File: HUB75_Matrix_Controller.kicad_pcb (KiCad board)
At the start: 4 copper layers, 59 x 53 mm, 52 parts, among them J1 USB_C_Receptacle_USB2.0_16P, J2 Barrel_Jack_MountingPin, J3 Screw_Terminal_01x02, J4 Micro_SD_Card_Det2, J5 SFH11-PBPC-D08-ST-BK, SW1 EN, SW2 BOOT, U1 LSM6DSOTR, U2 AMS1117-3.3, U3 USBLC6-2SC6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

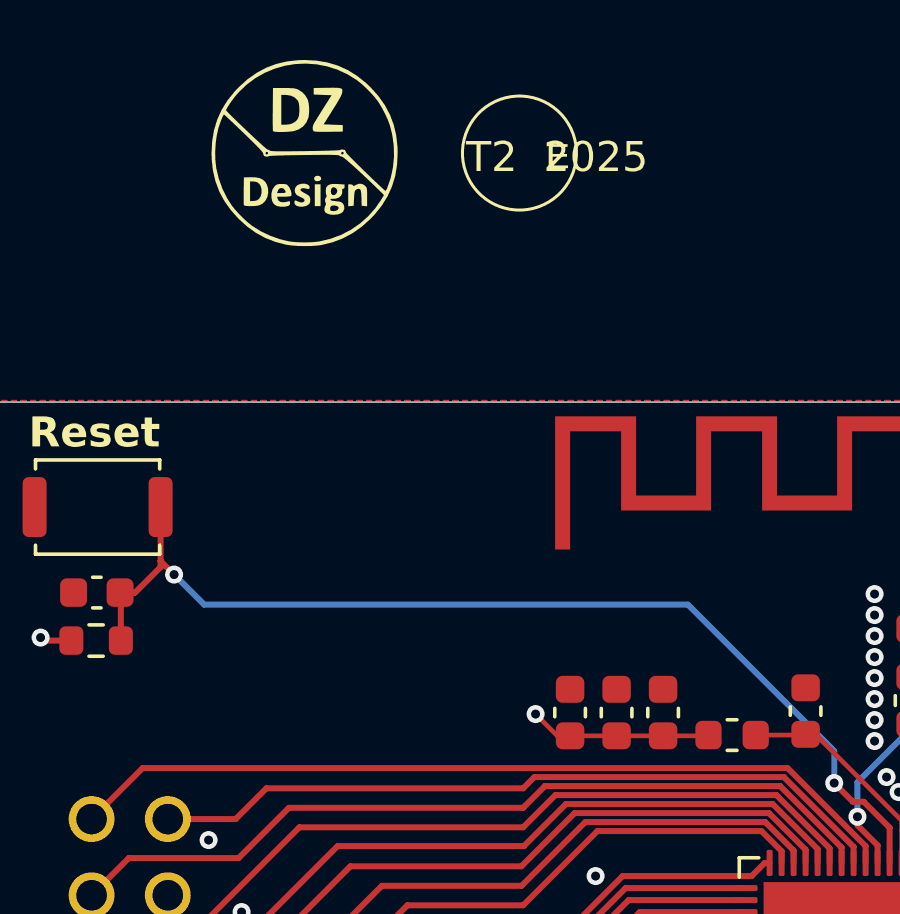
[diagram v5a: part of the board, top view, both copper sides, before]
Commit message: Removed level shifters | Added code examples
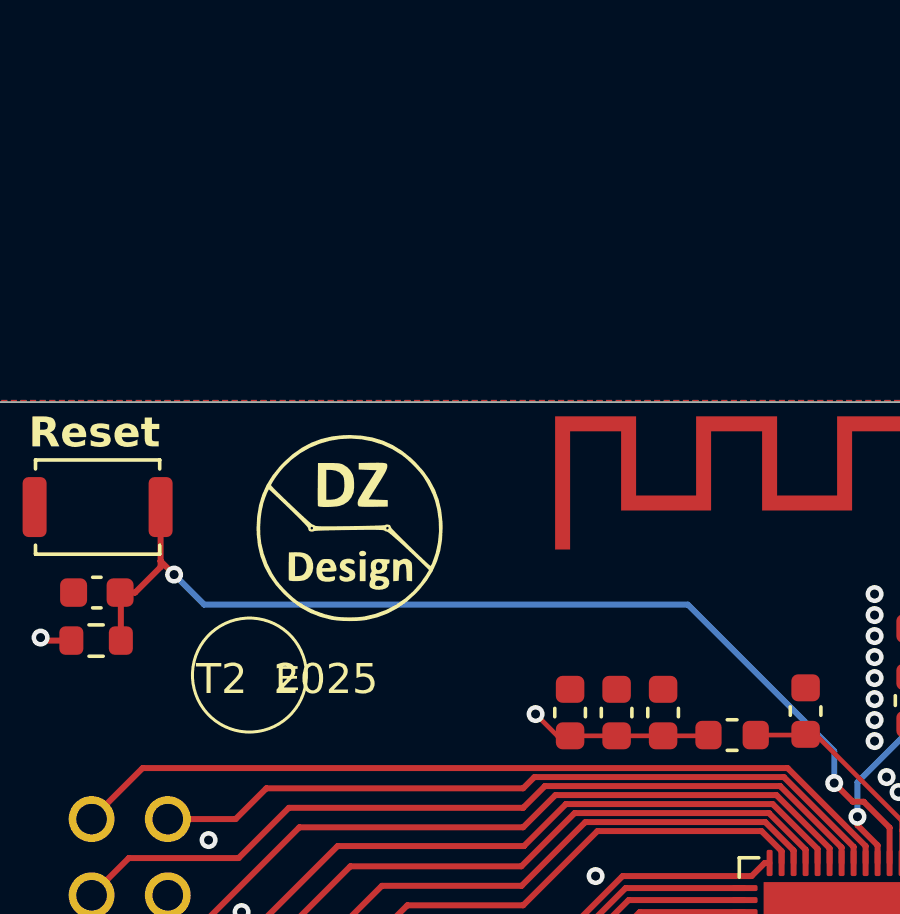
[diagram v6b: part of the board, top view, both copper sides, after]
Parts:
- moved G*** 12.6 mm to (133.0, 81.0)
